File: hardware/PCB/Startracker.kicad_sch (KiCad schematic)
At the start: 0 parts

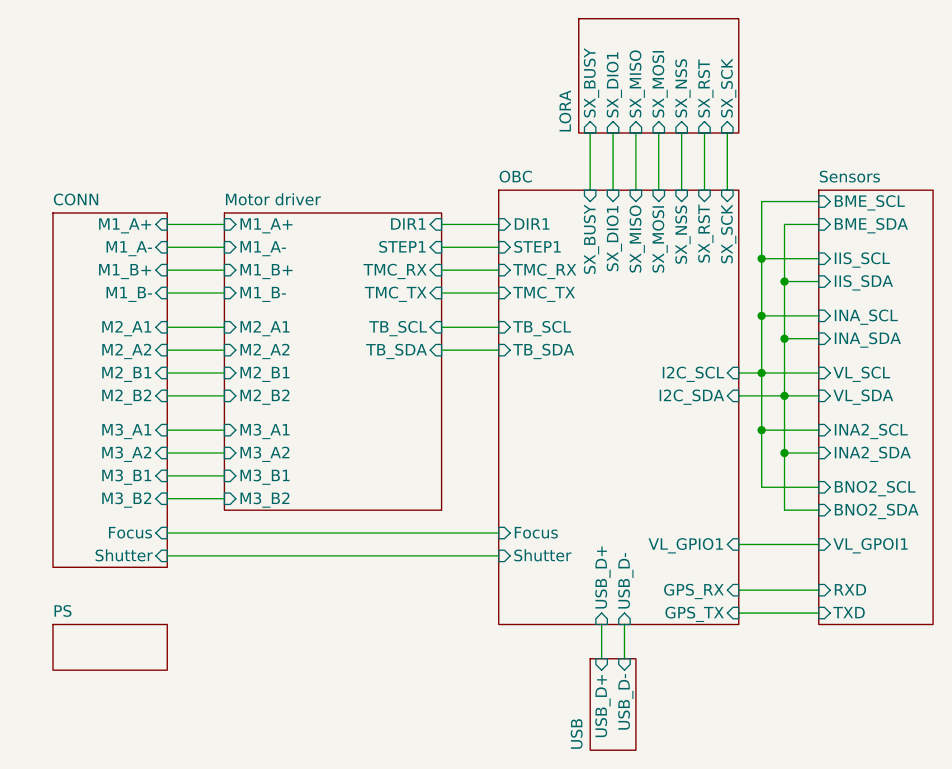
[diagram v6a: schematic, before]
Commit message: Removed polar azimuth motor driver from pcb
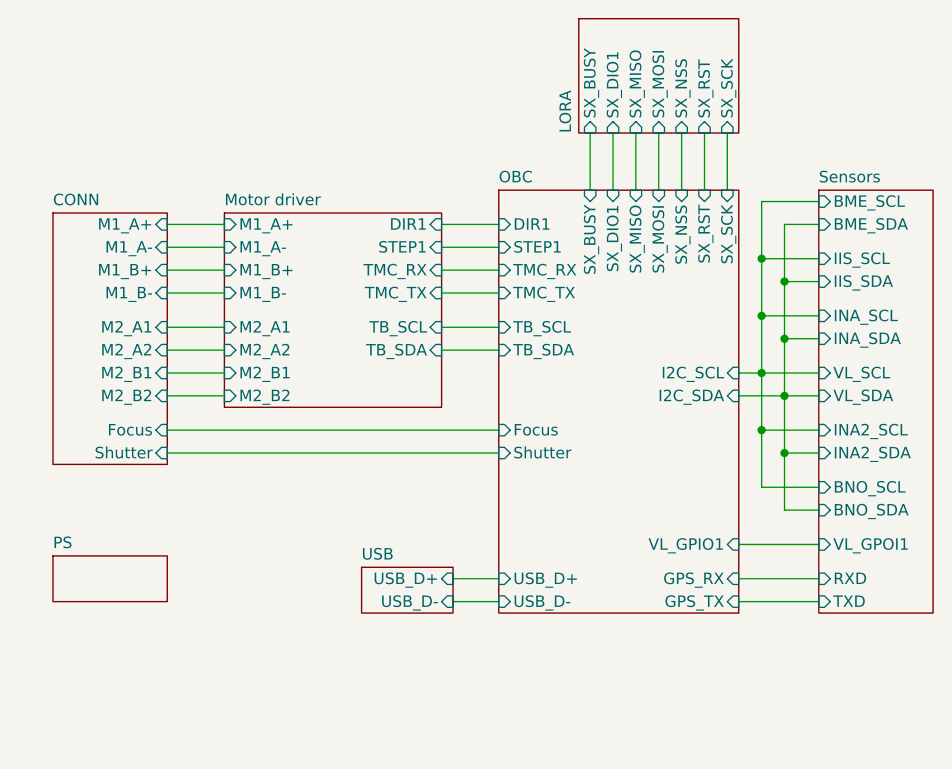
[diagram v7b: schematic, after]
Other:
- sheet CONN ports: added none; removed M3_A1, M3_A2, M3_B1, M3_B2
- sheet Motor driver ports: added none; removed M3_A1, M3_A2, M3_B1, M3_B2
- sheet Sensors ports: added BNO_SCL, BNO_SDA; removed BNO2_SCL, BNO2_SDA
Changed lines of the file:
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@@
 	(wire
 		(pts
-			(xy 62.23 64.77) (xy 68.58 64.77)
+			(xy 93.98 83.82) (xy 99.06 83.82)
 		)
 		(stroke
@@
 	(wire
 		(pts
-			(xy 62.23 76.2) (xy 99.06 76.2)
+			(xy 62.23 64.77) (xy 99.06 64.77)
 		)
 		(stroke
@@
 	(wire
 		(pts
+			(xy 125.73 83.82) (xy 134.62 83.82)
+		)
+		(stroke
+			(width 0)
+			(type default)
+		)
+	)
+	(wire
+		(pts
 			(xy 134.62 41.91) (xy 130.81 41.91)
 		)
@@
 	(wire
 		(pts
-			(xy 62.23 69.85) (xy 68.58 69.85)
-		)
-		(stroke
-			(width 0)
-			(type default)
-		)
-	)
-	(wire
-		(pts
 			(xy 62.23 41.91) (xy 68.58 41.91)
 		)
@@
 	(wire
 		(pts
-			(xy 113.03 86.36) (xy 113.03 90.17)
-		)
-		(stroke
-			(width 0)
-			(type default)
-		)
-	)
-	(wire
-		(pts
 			(xy 116.84 31.75) (xy 116.84 38.1)
 		)
@@
 	(wire
 		(pts
+			(xy 93.98 81.28) (xy 99.06 81.28)
+		)
+		(stroke
+			(width 0)
+			(type default)
+		)
+	)
+	(wire
+		(pts
 			(xy 62.23 49.53) (xy 68.58 49.53)
 		)
@@
 	(wire
 		(pts
-			(xy 62.23 67.31) (xy 68.58 67.31)
-		)
-		(stroke
-			(width 0)
-			(type default)
-		)
-	)
-	(wire
-		(pts
 			(xy 134.62 73.66) (xy 130.81 73.66)
 		)
@@
 	(wire
 		(pts
-			(xy 125.73 82.55) (xy 134.62 82.55)
+			(xy 125.73 81.28) (xy 134.62 81.28)
 		)
 		(stroke
@@
 	(wire
 		(pts
-			(xy 125.73 85.09) (xy 134.62 85.09)
-		)
-		(stroke
-			(width 0)
-			(type default)
-		)
-	)
-	(wire
-		(pts
 			(xy 128.27 64.77) (xy 128.27 71.12)
 		)
@@
 	(wire
 		(pts
-			(xy 62.23 72.39) (xy 68.58 72.39)
-		)
-		(stroke
-			(width 0)
-			(type default)
-		)
-	)
-	(wire
-		(pts
 			(xy 134.62 71.12) (xy 128.27 71.12)
 		)
@@
 	(wire
 		(pts
-			(xy 110.49 86.36) (xy 110.49 90.17)
-		)
-		(stroke
-			(width 0)
-			(type default)
-		)
-	)
-	(wire
-		(pts
-			(xy 62.23 78.74) (xy 99.06 78.74)
+			(xy 62.23 67.31) (xy 99.06 67.31)
 		)
 		(stroke
@@
 	(sheet
 		(at 49.53 40.64)
-		(size 12.7 39.37)
+		(size 12.7 27.94)
 		(exclude_from_sim no)
 		(in_bom yes)
@@
 		)
 		(property "Sheetfile" "conn.kicad_sch"
-			(at 49.53 80.5946 0)
+			(at 49.53 69.1646 0)
 			(effects
 				(font
@@
 			)
 		)
-		(pin "M3_A1" input
+		(pin "Focus" input
 			(at 62.23 64.77 0)
 			(effects
@@
 			)
 		)
-		(pin "M3_A2" input
+		(pin "Shutter" input
 			(at 62.23 67.31 0)
-			(effects
-				(font
-					(size 1.27 1.27)
-				)
-				(justify right)
-			)
-		)
-		(pin "M3_B1" input
-			(at 62.23 69.85 0)
-			(effects
-				(font
-					(size 1.27 1.27)
-				)
-				(justify right)
-			)
-		)
-		(pin "M3_B2" input
-			(at 62.23 72.39 0)
-			(effects
-				(font
-					(size 1.27 1.27)
-				)
-				(justify right)
-			)
-		)
-		(pin "Focus" input
-			(at 62.23 76.2 0)
-			(effects
-				(font
-					(size 1.27 1.27)
-				)
-				(justify right)
-			)
-		)
-		(pin "Shutter" input
-			(at 62.23 78.74 0)
 			(effects
 				(font
@@
 	(sheet
 		(at 68.58 40.64)
-		(size 24.13 33.02)
+		(size 24.13 21.59)
 		(exclude_from_sim no)
 		(in_bom yes)
@@
 		)
 		(property "Sheetfile" "motor_driver.kicad_sch"
-			(at 68.58 74.2446 0)
+			(at 68.58 62.8146 0)
 			(effects
 				(font
@@
 		(pin "M2_B2" input
 			(at 68.58 60.96 180)
-			(effects
-				(font
-					(size 1.27 1.27)
-				)
-				(justify left)
-			)
-		)
-		(pin "M3_A1" input
-			(at 68.58 64.77 180)
-			(effects
-				(font
-					(size 1.27 1.27)
-				)
-				(justify left)
-			)
-		)
-		(pin "M3_A2" input
-			(at 68.58 67.31 180)
-			(effects
-				(font
-					(size 1.27 1.27)
-				)
-				(justify left)
-			)
-		)
-		(pin "M3_B1" input
-			(at 68.58 69.85 180)
-			(effects
-				(font
-					(size 1.27 1.27)
-				)
-				(justify left)
-			)
-		)
-		(pin "M3_B2" input
-			(at 68.58 72.39 180)
 			(effects
 				(font
@@
 	)
 	(sheet
-		(at 109.22 90.17)
-		(size 5.08 10.16)
+		(at 83.82 80.01)
+		(size 10.16 5.08)
 		(exclude_from_sim no)
 		(in_bom yes)
@@
 		)
 		(property "Sheetname" "USB"
-			(at 108.5084 100.33 90)
+			(at 83.82 79.2984 0)
 			(effects
 				(font
@@
 		)
 		(property "Sheetfile" "usb.kicad_sch"
-			(at 114.8846 100.33 90)
+			(at 83.82 85.6746 0)
 			(effects
 				(font
@@
 		)
 		(pin "USB_D+" input
-			(at 110.49 90.17 90)
+			(at 93.98 81.28 0)
 			(effects
 				(font
@@
 		)
 		(pin "USB_D-" input
-			(at 113.03 90.17 90)
+			(at 93.98 83.82 0)
 			(effects
 				(font
@@
 	)
 	(sheet
-		(at 49.53 86.36)
+		(at 49.53 78.74)
 		(size 12.7 5.08)
 		(exclude_from_sim no)
@@
 		)
 		(property "Sheetname" "PS"
-			(at 49.53 85.6484 0)
+			(at 49.53 78.0284 0)
 			(effects
 				(font
@@
 		)
 		(property "Sheetfile" "ps.kicad_sch"
-			(at 49.53 92.0246 0)
+			(at 49.53 84.4046 0)
 			(effects
 				(font
@@
 	(sheet
 		(at 99.06 38.1)
-		(size 26.67 48.26)
+		(size 26.67 46.99)
 		(exclude_from_sim no)
 		(in_bom yes)
@@
 		)
 		(property "Sheetfile" "obc.kicad_sch"
-			(at 99.06 86.9446 0)
+			(at 99.06 85.6746 0)
 			(effects
 				(font
@@
 		)
 		(pin "GPS_RX" input
-			(at 125.73 82.55 0)
+			(at 125.73 81.28 0)
 			(effects
 				(font
@@
 		)
 		(pin "GPS_TX" input
-			(at 125.73 85.09 0)
+			(at 125.73 83.82 0)
 			(effects
 				(font
@@
 		)
 		(pin "USB_D+" input
-			(at 110.49 86.36 270)
+			(at 99.06 81.28 180)
 			(effects
 				(font
@@
 		)
 		(pin "USB_D-" input
-			(at 113.03 86.36 270)
+			(at 99.06 83.82 180)
 			(effects
 				(font
@@
 		)
 		(pin "Focus" input
-			(at 99.06 76.2 180)
+			(at 99.06 64.77 180)
 			(effects
 				(font
@@
 		)
 		(pin "Shutter" input
-			(at 99.06 78.74 180)
+			(at 99.06 67.31 180)
 			(effects
 				(font
@@
 	(sheet
 		(at 134.62 38.1)
-		(size 12.7 48.26)
+		(size 12.7 46.99)
 		(exclude_from_sim no)
 		(in_bom yes)
@@
 		)
 		(property "Sheetfile" "sensors.kicad_sch"
-			(at 134.62 86.9446 0)
+			(at 134.62 85.6746 0)
 			(effects
 				(font
@@
 		)
 		(pin "RXD" input
-			(at 134.62 82.55 180)
+			(at 134.62 81.28 180)
 			(effects
 				(font
@@
 		)
 		(pin "TXD" input
-			(at 134.62 85.09 180)
+			(at 134.62 83.82 180)
 			(effects
 				(font
@@
 			)
 		)
-		(pin "BNO2_SCL" input
+		(pin "BNO_SCL" input
 			(at 134.62 71.12 180)
 			(effects
@@
 			)
 		)
-		(pin "BNO2_SDA" input
+		(pin "BNO_SDA" input
 			(at 134.62 73.66 180)
 			(effects
